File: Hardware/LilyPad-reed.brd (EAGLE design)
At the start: 7.6 x 33.4 mm, 6 parts

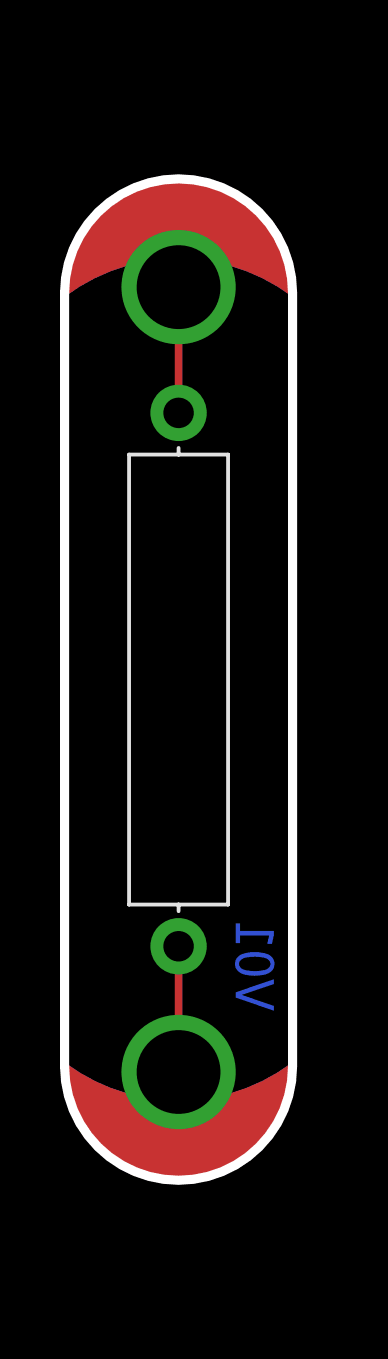
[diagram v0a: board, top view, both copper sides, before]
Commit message: post-review edits
added PTH pins
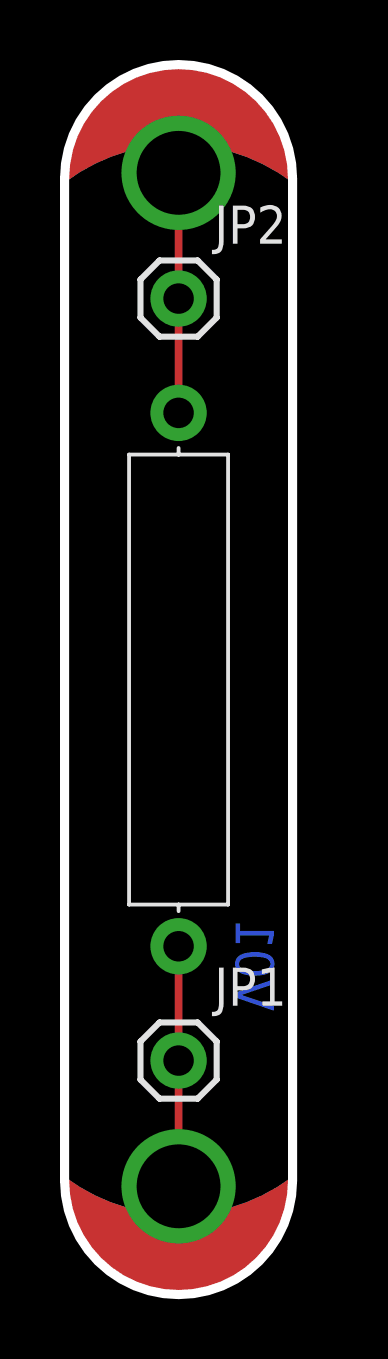
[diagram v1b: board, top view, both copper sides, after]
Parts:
- added JP1, JP2: (no value), SparkFun-Connectors:1X01
- moved SLIDEOFF 3.81 mm to (0.00, -16.6)
- moved SLIDEON 3.81 mm to (0.00, 16.6)
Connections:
- net N$1: now also JP1.1
- net N$2: now also JP2.1
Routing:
- net N$2: track 4.19 -> 8.00 mm
- net N$1: track 4.19 -> 8.00 mm
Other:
- board size 7.6 x 33.4 mm -> 7.6 x 41 mm
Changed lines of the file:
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@@
 <grid distance="0.05" unitdist="inch" unit="inch" style="lines" multiple="1" display="yes" altdistance="0.005" altunitdist="inch" altunit="inch"/>
 <layers>
-<layer number="1" name="Top" color="4" fill="1" visible="no" active="yes"/>
+<layer number="1" name="Top" color="4" fill="1" visible="yes" active="yes"/>
 <layer number="2" name="Route2" color="1" fill="3" visible="no" active="yes"/>
 <layer number="15" name="Route15" color="4" fill="6" visible="no" active="yes"/>
@@
 <layer number="19" name="Unrouted" color="6" fill="1" visible="yes" active="yes"/>
 <layer number="20" name="Dimension" color="6" fill="1" visible="yes" active="yes"/>
-<layer number="21" name="tPlace" color="16" fill="1" visible="no" active="yes"/>
+<layer number="21" name="tPlace" color="16" fill="1" visible="yes" active="yes"/>
 <layer number="22" name="bPlace" color="14" fill="1" visible="yes" active="yes"/>
-<layer number="23" name="tOrigins" color="15" fill="1" visible="no" active="yes"/>
+<layer number="23" name="tOrigins" color="15" fill="1" visible="yes" active="yes"/>
 <layer number="24" name="bOrigins" color="15" fill="1" visible="yes" active="yes"/>
 <layer number="25" name="tNames" color="7" fill="1" visible="no" active="yes"/>
@@
 <layer number="43" name="vRestrict" color="2" fill="10" visible="no" active="yes"/>
 <layer number="44" name="Drills" color="7" fill="1" visible="no" active="yes"/>
-<layer number="45" name="Holes" color="7" fill="1" visible="no" active="yes"/>
+<layer number="45" name="Holes" color="7" fill="1" visible="yes" active="yes"/>
 <layer number="46" name="Milling" color="3" fill="1" visible="no" active="yes"/>
 <layer number="47" name="Measures" color="7" fill="1" visible="no" active="yes"/>
-<layer number="51" name="tDocu" color="6" fill="1" visible="no" active="yes"/>
+<layer number="51" name="tDocu" color="6" fill="1" visible="yes" active="yes"/>
 <layer number="3" name="Route3" color="4" fill="3" visible="no" active="no"/>
 <layer number="4" name="Route4" color="1" fill="4" visible="no" active="no"/>
@@
 <layer number="56" name="wert" color="7" fill="1" visible="no" active="no"/>
 <layer number="57" name="tCAD" color="7" fill="1" visible="no" active="no"/>
+<layer number="90" name="Modules" color="5" fill="1" visible="no" active="no"/>
 <layer number="91" name="Nets" color="2" fill="1" visible="no" active="no"/>
 <layer number="92" name="Busses" color="1" fill="1" visible="no" active="no"/>
@@
 <board>
 <plain>
-<wire x1="-3.8" y1="12.89" x2="3.8" y2="12.89" width="0.3048" layer="20" curve="-180"/>
-<wire x1="3.8" y1="-12.89" x2="-3.8" y2="-12.89" width="0.3048" layer="20" curve="-180"/>
-<wire x1="-3.8" y1="12.89" x2="-3.8" y2="-12.89" width="0.3048" layer="20"/>
-<wire x1="3.8" y1="12.89" x2="3.8" y2="-12.89" width="0.3048" layer="20"/>
+<wire x1="-3.8" y1="16.7" x2="3.8" y2="16.7" width="0.3048" layer="20" curve="-180"/>
+<wire x1="3.8" y1="-16.7" x2="-3.8" y2="-16.7" width="0.3048" layer="20" curve="-180"/>
+<wire x1="-3.8" y1="16.7" x2="-3.8" y2="-16.7" width="0.3048" layer="20"/>
+<wire x1="3.8" y1="16.7" x2="3.8" y2="-16.7" width="0.3048" layer="20"/>
 <text x="-60.96" y="0" size="1.778" layer="51" font="vector" ratio="15">Dia Campbell</text>
 <text x="1.905" y="-11.049" size="1.27" layer="16" font="vector" ratio="15" rot="MR90">V01</text>
@@
 </autorouter>
 <elements>
-<element name="SLIDEOFF" library="LilyPad-Wearables" package="PETAL-MEDIUM-2SIDE" value="SEWTAP8" x="0" y="-12.827"/>
-<element name="SLIDEON" library="LilyPad-Wearables" package="PETAL-MEDIUM-2SIDE" value="SEWTAP8" x="0" y="12.827" rot="R180"/>
+<element name="SLIDEOFF" library="LilyPad-Wearables" package="PETAL-MEDIUM-2SIDE" value="SEWTAP8" x="0" y="-16.637"/>
+<element name="SLIDEON" library="LilyPad-Wearables" package="PETAL-MEDIUM-2SIDE" value="SEWTAP8" x="0" y="16.637" rot="R180"/>
 <element name="REED" library="SparkFun-Electromechanical" package="REED_SWITCH_PLASTIC" value="SWITCH-MOMENTARY-2PTH_REED2" x="0" y="0" rot="R270"/>
 <element name="U$1" library="LilyPad-Wearables" package="LOGO-LILYPAD" value="LOGO-LPLP" x="0.127" y="-1.778" rot="MR90"/>
@@
 </element>
 <element name="LOGO1" library="SparkFun-Aesthetics" package="OSHW-LOGO-S" value="OSHW-LOGOS" x="0" y="5.461" rot="MR90"/>
+<element name="JP1" library="SparkFun-Connectors" package="1X01" value="" x="0" y="-12.7"/>
+<element name="JP2" library="SparkFun-Connectors" package="1X01" value="" x="0" y="12.7"/>
 </elements>
 <signals>
@@
 <contactref element="SLIDEOFF" pad="1"/>
 <contactref element="REED" pad="P$2"/>
-<wire x1="0" y1="-8.89" x2="0" y2="-13.081" width="0.254" layer="1"/>
+<contactref element="JP1" pad="1"/>
+<wire x1="0" y1="-16.891" x2="0" y2="-12.7" width="0.254" layer="1"/>
+<wire x1="0" y1="-8.89" x2="0" y2="-12.7" width="0.254" layer="1"/>
 </signal>
 <signal name="N$2">
 <contactref element="REED" pad="P$1"/>
 <contactref element="SLIDEON" pad="1"/>
-<wire x1="0" y1="8.89" x2="0" y2="13.081" width="0.254" layer="1"/>
+<contactref element="JP2" pad="1"/>
+<wire x1="0" y1="16.891" x2="0" y2="12.7" width="0.254" layer="1"/>
+<wire x1="0" y1="8.89" x2="0" y2="12.7" width="0.254" layer="1"/>
 </signal>
 </signals>

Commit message: Increased trace width, added dimension
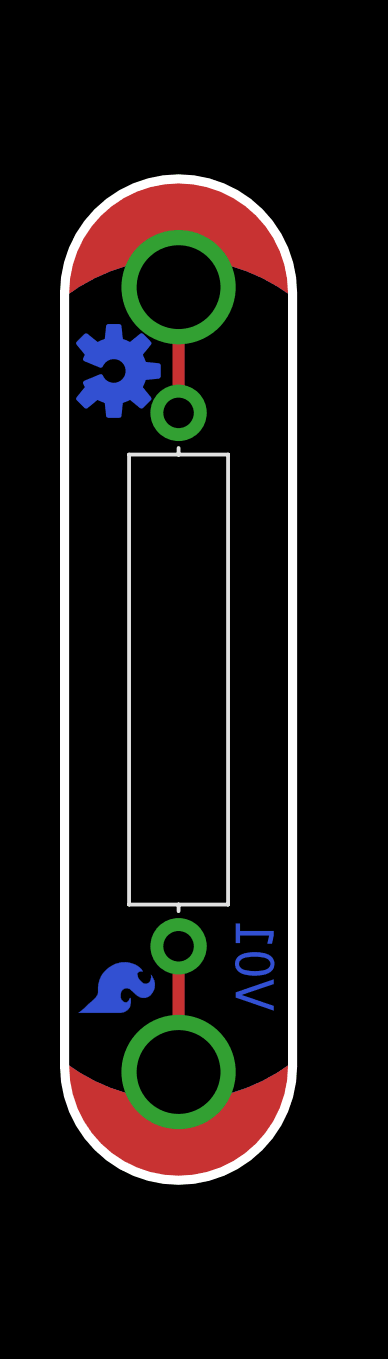
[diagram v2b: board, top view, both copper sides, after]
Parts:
- removed JP1, JP2: (no value), SparkFun-Connectors:1X01
- added LOGO2: SFE_LOGO_FLAME.1COP, SparkFun-Aesthetics:SFE_LOGO_FLAME_COPPER_.1
- LOGO1: value OSHW-LOGOS -> OSHW-LOGOS-COPPER; device SparkFun-Aesthetics:OSHW-LOGO-S -> SparkFun-Aesthetics:OSHW-LOGO-S_COPPER
- moved LOGO1 5.29 mm to (-2.16, 10.3)
- moved SLIDEOFF 3.81 mm to (0.00, -12.8)
- moved SLIDEON 3.81 mm to (0.00, 12.8)
- moved U$1 1.65 mm to (0.13, -0.13)
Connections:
- net N$1: no longer JP1.1
- net N$2: no longer JP2.1
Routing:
- net N$2: track 8.00 -> 4.19 mm
- net N$1: track 8.00 -> 4.19 mm
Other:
- board size 7.6 x 41 mm -> 7.6 x 33.4 mm
- board text added: "Dimensions in inches"
- board text added: "purple 0.08mm"
- board text added: "purple 0.8mm"
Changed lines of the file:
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@@
 <layer number="18" name="Vias" color="2" fill="1" visible="yes" active="yes"/>
 <layer number="19" name="Unrouted" color="6" fill="1" visible="yes" active="yes"/>
-<layer number="20" name="Dimension" color="6" fill="1" visible="yes" active="yes"/>
+<layer number="20" name="Dimension" color="15" fill="1" visible="yes" active="yes"/>
 <layer number="21" name="tPlace" color="16" fill="1" visible="yes" active="yes"/>
 <layer number="22" name="bPlace" color="14" fill="1" visible="yes" active="yes"/>
@@
 <layer number="56" name="wert" color="7" fill="1" visible="no" active="no"/>
 <layer number="57" name="tCAD" color="7" fill="1" visible="no" active="no"/>
+<layer number="59" name="tCarbon" color="7" fill="1" visible="no" active="no"/>
+<layer number="60" name="bCarbon" color="7" fill="1" visible="no" active="no"/>
 <layer number="90" name="Modules" color="5" fill="1" visible="no" active="no"/>
 <layer number="91" name="Nets" color="2" fill="1" visible="no" active="no"/>
@@
 <layer number="127" name="_tValues" color="7" fill="1" visible="no" active="no"/>
 <layer number="128" name="_bValues" color="7" fill="1" visible="no" active="no"/>
+<layer number="129" name="Mask" color="7" fill="1" visible="no" active="yes"/>
 <layer number="131" name="tAdjust" color="7" fill="1" visible="no" active="no"/>
 <layer number="132" name="bAdjust" color="7" fill="1" visible="no" active="no"/>
@@
 <layer number="251" name="SMDround" color="12" fill="11" visible="no" active="no"/>
 <layer number="254" name="cooling" color="7" fill="1" visible="no" active="no"/>
+<layer number="255" name="routoute" color="7" fill="1" visible="no" active="yes"/>
 </layers>
 <board>
 <plain>
-<wire x1="-3.8" y1="16.7" x2="3.8" y2="16.7" width="0.3048" layer="20" curve="-180"/>
-<wire x1="3.8" y1="-16.7" x2="-3.8" y2="-16.7" width="0.3048" layer="20" curve="-180"/>
-<wire x1="-3.8" y1="16.7" x2="-3.8" y2="-16.7" width="0.3048" layer="20"/>
-<wire x1="3.8" y1="16.7" x2="3.8" y2="-16.7" width="0.3048" layer="20"/>
+<wire x1="-3.8" y1="12.89" x2="3.8" y2="12.89" width="0.3048" layer="20" curve="-180"/>
+<wire x1="3.8" y1="-12.89" x2="-3.8" y2="-12.89" width="0.3048" layer="20" curve="-180"/>
+<wire x1="-3.8" y1="12.89" x2="-3.8" y2="-12.89" width="0.3048" layer="20"/>
+<wire x1="3.8" y1="12.89" x2="3.8" y2="-12.89" width="0.3048" layer="20"/>
 <text x="-60.96" y="0" size="1.778" layer="51" font="vector" ratio="15">Dia Campbell</text>
 <text x="1.905" y="-11.049" size="1.27" layer="16" font="vector" ratio="15" rot="MR90">V01</text>
+<text x="6.35" y="22.86" size="1.778" layer="52" font="vector" ratio="15">purple 0.08mm</text>
+<text x="-10.16" y="21.59" size="1.778" layer="51" font="vector" ratio="15">purple 0.8mm</text>
+<dimension x1="-3.8" y1="12.89" x2="3.81" y2="11.43" x3="0.005" y3="-21.59" textsize="1.778" textratio="15" layer="51" dtype="horizontal" unit="inch"/>
+<dimension x1="0" y1="16.637" x2="0.127" y2="-16.637" x3="11.43" y3="0" textsize="1.778" textratio="15" layer="51" dtype="vertical" unit="inch"/>
+<text x="-13.97" y="-26.67" size="1.778" layer="51" font="vector" ratio="15">Dimensions in inches</text>
 </plain>
 <attributes>
@@
 </class>
 </classes>
-<designrules name="SparkFun">
+<designrules name="SparkFun-2-layer">
 <description language="en">&lt;b&gt;EAGLE Design Rules&lt;/b&gt;
 &lt;p&gt;
@@
 <param name="mdViaViaSameLayer" value="8mil"/>
 <param name="mnLayersViaInSmd" value="2"/>
-<param name="mdCopperDimension" value="10mil"/>
+<param name="mdCopperDimension" value="8mil"/>
 <param name="mdDrill" value="8mil"/>
 <param name="mdSmdStop" value="0mil"/>
-<param name="msWidth" value="8mil"/>
-<param name="msDrill" value="20mil"/>
+<param name="msWidth" value="7mil"/>
+<param name="msDrill" value="15mil"/>
 <param name="msMicroVia" value="9.99mm"/>
 <param name="msBlindViaRatio" value="0.5"/>
@@
 <param name="mlMinCreamFrame" value="0mil"/>
 <param name="mlMaxCreamFrame" value="0mil"/>
-<param name="mlViaStopLimit" value="25mil"/>
+<param name="mlViaStopLimit" value="20mil"/>
 <param name="srRoundness" value="0"/>
 <param name="srMinRoundness" value="0mil"/>
@@
 <param name="dpGapFactor" value="2.5"/>
 <param name="checkGrid" value="0"/>
-<param name="checkAngle" value="0"/>
+<param name="checkAngle" value="1"/>
 <param name="checkFont" value="1"/>
 <param name="checkRestrict" value="1"/>
@@
 </autorouter>
 <elements>
-<element name="SLIDEOFF" library="LilyPad-Wearables" package="PETAL-MEDIUM-2SIDE" value="SEWTAP8" x="0" y="-16.637"/>
-<element name="SLIDEON" library="LilyPad-Wearables" package="PETAL-MEDIUM-2SIDE" value="SEWTAP8" x="0" y="16.637" rot="R180"/>
+<element name="SLIDEOFF" library="LilyPad-Wearables" package="PETAL-MEDIUM-2SIDE" value="SEWTAP8" x="0" y="-12.827"/>
+<element name="SLIDEON" library="LilyPad-Wearables" package="PETAL-MEDIUM-2SIDE" value="SEWTAP8" x="0" y="12.827" rot="R180"/>
 <element name="REED" library="SparkFun-Electromechanical" package="REED_SWITCH_PLASTIC" value="SWITCH-MOMENTARY-2PTH_REED2" x="0" y="0" rot="R270"/>
-<element name="U$1" library="LilyPad-Wearables" package="LOGO-LILYPAD" value="LOGO-LPLP" x="0.127" y="-1.778" rot="MR90"/>
+<element name="U$1" library="LilyPad-Wearables" package="LOGO-LILYPAD" value="LOGO-LPLP" x="0.127" y="-0.127" rot="MR90"/>
 <element name="FRAME1" library="SparkFun-Aesthetics" package="CREATIVE_COMMONS" value="" x="-91.73185625" y="0">
 <attribute name="VERSION" value="v01" x="-91.73185625" y="0" size="1.778" layer="27" display="off"/>
 <attribute name="DESIGNER" value="NAME" x="-91.73185625" y="0" size="1.778" layer="27" display="off"/>
 </element>
-<element name="LOGO1" library="SparkFun-Aesthetics" package="OSHW-LOGO-S" value="OSHW-LOGOS" x="0" y="5.461" rot="MR90"/>
-<element name="JP1" library="SparkFun-Connectors" package="1X01" value="" x="0" y="-12.7"/>
-<element name="JP2" library="SparkFun-Connectors" package="1X01" value="" x="0" y="12.7"/>
+<element name="LOGO1" library="SparkFun-Aesthetics" package="OSHW-LOGO-S_COPPER" value="OSHW-LOGOS-COPPER" x="-2.159" y="10.287" rot="MR90"/>
+<element name="LOGO2" library="SparkFun-Aesthetics" package="SFE_LOGO_FLAME_COPPER_.1" value="SFE_LOGO_FLAME.1COP" x="-3.683" y="-11.43" rot="MR90"/>
 </elements>
 <signals>
@@
 <contactref element="SLIDEOFF" pad="1"/>
 <contactref element="REED" pad="P$2"/>
-<contactref element="JP1" pad="1"/>
-<wire x1="0" y1="-16.891" x2="0" y2="-12.7" width="0.254" layer="1"/>
-<wire x1="0" y1="-8.89" x2="0" y2="-12.7" width="0.254" layer="1"/>
+<wire x1="0" y1="-13.081" x2="0" y2="-8.89" width="0.4064" layer="1"/>
 </signal>
 <signal name="N$2">
 <contactref element="REED" pad="P$1"/>
 <contactref element="SLIDEON" pad="1"/>
-<contactref element="JP2" pad="1"/>
-<wire x1="0" y1="16.891" x2="0" y2="12.7" width="0.254" layer="1"/>
-<wire x1="0" y1="8.89" x2="0" y2="12.7" width="0.254" layer="1"/>
+<wire x1="0" y1="13.081" x2="0" y2="8.89" width="0.4064" layer="1"/>
 </signal>
 </signals>
